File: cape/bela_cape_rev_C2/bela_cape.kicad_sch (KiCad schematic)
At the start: 34 parts, among them J1 Conn_01x02, J10 Conn_01x04, J11 Conn_01x02, J2 Conn_01x04, J3 Conn_01x03, J4 Conn_01x03, J5 Conn_01x02, J6 Conn_01x02, J7 Conn_01x10, J8 Conn_01x10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

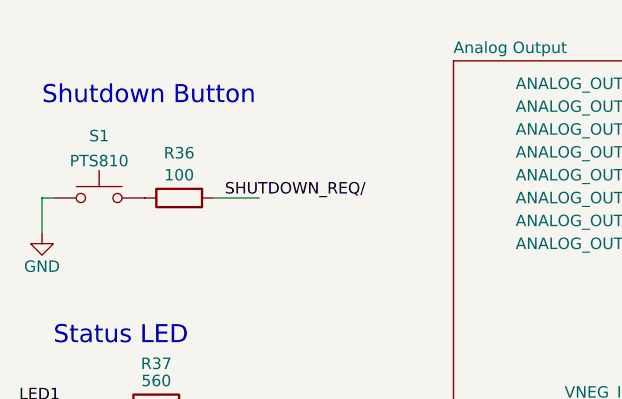
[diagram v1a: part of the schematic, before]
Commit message: A few edits to C2 cape
(cherry picked from commit 42570a0d57f5cd6d8ff56c36d77f2d0b211cc62f)
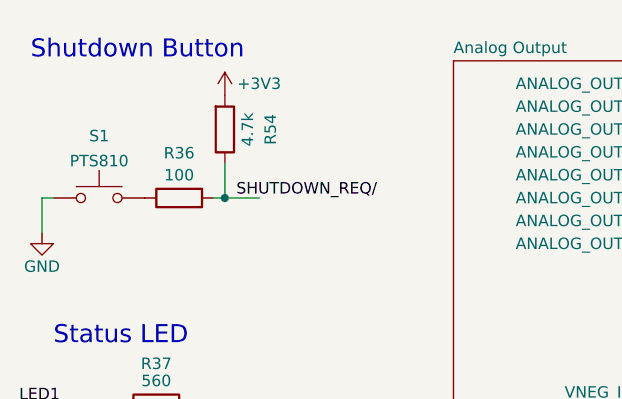
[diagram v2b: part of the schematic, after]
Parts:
- added R54: 4.7k, Resistor_SMD:R_0603_1608Metric, symbol Device:R
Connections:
- net +3V3: now also R54.2
- net SHUTDOWN_REQ/: now also R54.1
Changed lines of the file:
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@@
     (company "Augmented Instruments Ltd.")
   )
+  (junction (at 44.45 38.1) (diameter 0) (color 0 0 0 0)
+  )
   (junction (at 198.12 157.48) (diameter 0) (color 0 0 0 0)
   )
@@
     (stroke (width 0) (type default) (color 0 0 0 0))
   )
-  (wire (pts (xy 43.18 38.1) (xy 48.26 38.1))
+  (wire (pts (xy 43.18 38.1) (xy 44.45 38.1))
     (stroke (width 0) (type default) (color 0 0 0 0))
   )
@@
     (stroke (width 0) (type default) (color 0 0 0 0))
   )
+  (wire (pts (xy 44.45 34.29) (xy 44.45 38.1))
+    (stroke (width 0) (type default) (color 0 0 0 0))
+  )
   (wire (pts (xy 200.66 71.12) (xy 203.2 71.12))
     (stroke (width 0) (type default) (color 0 0 0 0))
@@
   )
   (wire (pts (xy 198.12 30.48) (xy 203.2 30.48))
+    (stroke (width 0) (type default) (color 0 0 0 0))
+  )
+  (wire (pts (xy 44.45 38.1) (xy 48.26 38.1))
     (stroke (width 0) (type default) (color 0 0 0 0))
   )
@@
     (effects (font (size 2 2)) (justify left bottom))
   )
-  (text "Shutdown Button" (at 24.13 27.94 0)
+  (text "Shutdown Button" (at 22.86 22.86 0)
     (effects (font (size 2 2)) (justify left bottom))
   )
@@
     (effects (font (size 1.27 1.27)) (justify left bottom))
   )
-  (label "SHUTDOWN_REQ{slash}" (at 44.45 38.1 0)
+  (label "SHUTDOWN_REQ{slash}" (at 45.72 38.1 0)
     (effects (font (size 1.27 1.27)) (justify left bottom))
   )
@@
     )
     (property "Datasheet" "~" (id 3) (at 118.11 59.69 0)
+      (effects (font (size 1.27 1.27)) hide)
+    )
+    (pin "1")
+    (pin "2")
+  )
+  (symbol (lib_id "Device:R") (at 44.45 30.48 0) (mirror x) (unit 1)
+    (in_bom yes) (on_board yes)
+    (property "Reference" "R54" (id 0) (at 49.53 30.48 90))
+    (property "Value" "4.7k" (id 1) (at 46.99 30.48 90))
+    (property "Footprint" "Resistor_SMD:R_0603_1608Metric" (id 2) (at 42.672 30.48 90)
+      (effects (font (size 1.27 1.27)) hide)
+    )
+    (property "Datasheet" "~" (id 3) (at 44.45 30.48 0)
       (effects (font (size 1.27 1.27)) hide)
     )
@@
     (pin "2")
   )
+  (symbol (lib_id "power:+3V3") (at 44.45 26.67 0) (unit 1)
+    (in_bom yes) (on_board yes)
+    (property "Reference" "#PWR0102" (id 0) (at 44.45 30.48 0)
+      (effects (font (size 1.27 1.27)) hide)
+    )
+    (property "Value" "+3V3" (id 1) (at 48.26 25.4 0))
+    (property "Footprint" "" (id 2) (at 44.45 26.67 0)
+      (effects (font (size 1.27 1.27)) hide)
+    )
+    (property "Datasheet" "" (id 3) (at 44.45 26.67 0)
+      (effects (font (size 1.27 1.27)) hide)
+    )
+    (pin "1")
+  )
   (symbol (lib_id "Device:R") (at 107.95 38.1 90) (mirror x) (unit 1)
     (in_bom yes) (on_board yes)
@@
       (reference "#PWR0101") (unit 1) (value "GNDA") (footprint "")
     )
+    (path "/aaeb80f6-d336-4df0-9842-d71cbcf50d00"
+      (reference "#PWR0102") (unit 1) (value "+3V3") (footprint "")
+    )
     (path "/9e34013b-8051-4e0b-88b6-b650bff5b520/c65d32c7-ac41-4f0d-bce7-f5dff0acf9f9"
       (reference "C1") (unit 1) (value "47uF") (footprint "Capacitor_SMD:C_1206_3216Metric")
@@
       (reference "R53") (unit 1) (value "330") (footprint "Resistor_SMD:R_0603_1608Metric")
     )
+    (path "/06f26ea1-7be2-4ad6-ad71-5ec05562113a"
+      (reference "R54") (unit 1) (value "4.7k") (footprint "Resistor_SMD:R_0603_1608Metric")
+    )
     (path "/63b54547-a58e-47a7-8ea4-655fb9be79b4"
